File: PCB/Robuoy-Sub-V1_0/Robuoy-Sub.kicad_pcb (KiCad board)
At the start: 4 copper layers, 100 x 80 mm, 160 parts, among them J101 1051330011, J102 Display, J103 LEDSTRIP, J104 SW1, J105 SW2, J201 Accu, J202 ESC SB POWER, J203 ESC BB POWER, J401 ESC-BB, J402 ESC-SB, J501 GPS, J601 Conn_Coaxial, J701 LED1, J702 LED2, J703 LED3, J704 SW1, J705 SW3, J706 SW2, J707 3.3V switch, J708 Vbatt switch, J709 MainswitchLeds, J901 Display, Q101 2N7002, Q102 2N7002, Q201 NCE01P30K, Q701 MMBT5551L, Q702 MMBT5551L, Q703 MMBT5551L, Q704 MMBT5551L, SW101 ~{BOOT}, SW102 ~{RESET}, SW201 ON/OFF, U101 SRV05-4, U102 CP2104-F03-GMR, U103 ESP32-WROOM-32E_(visible_peri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, U201 AP7363, U202 XL1509-5.0E1, U301 LSM303C, U601 Ai-Thinker-Ra-01, U701 MCP23017_SS, U801 LIS2HH12

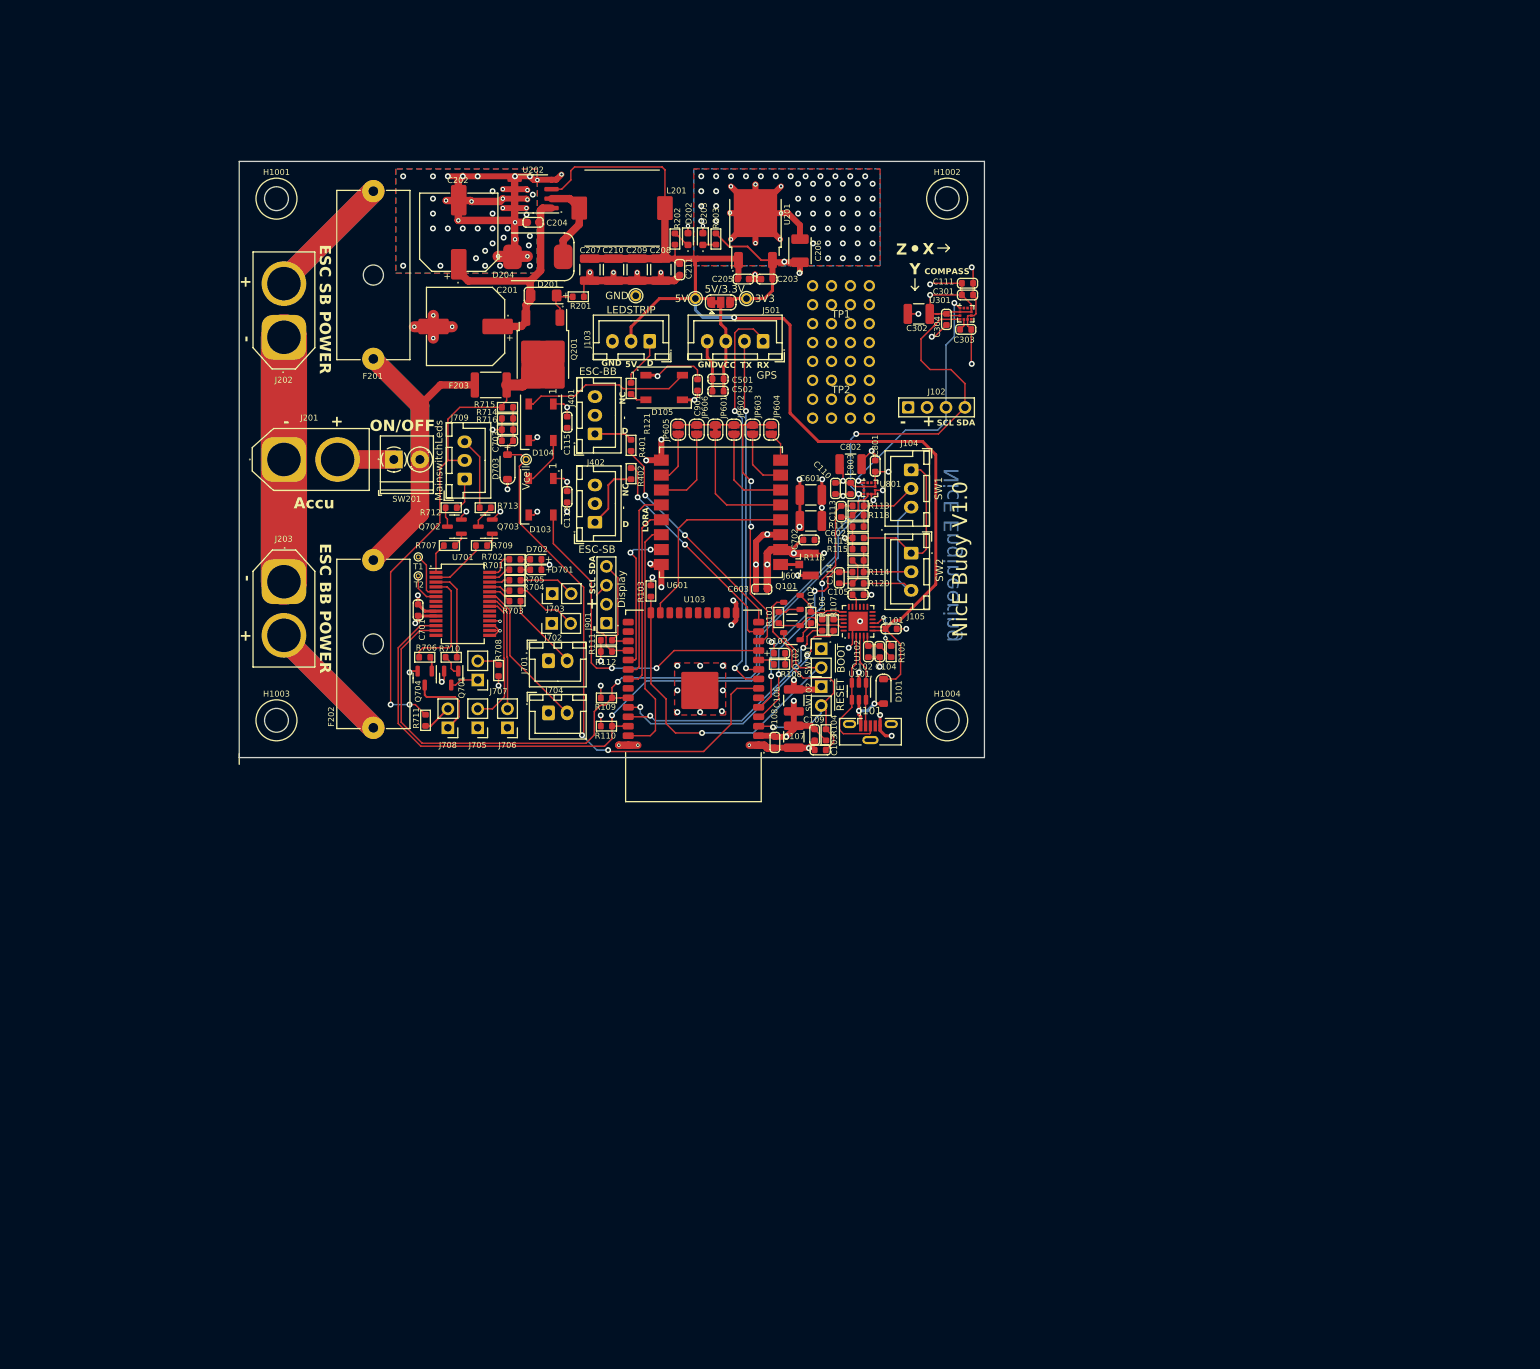
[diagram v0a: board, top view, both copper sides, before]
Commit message: Sub ready for routing
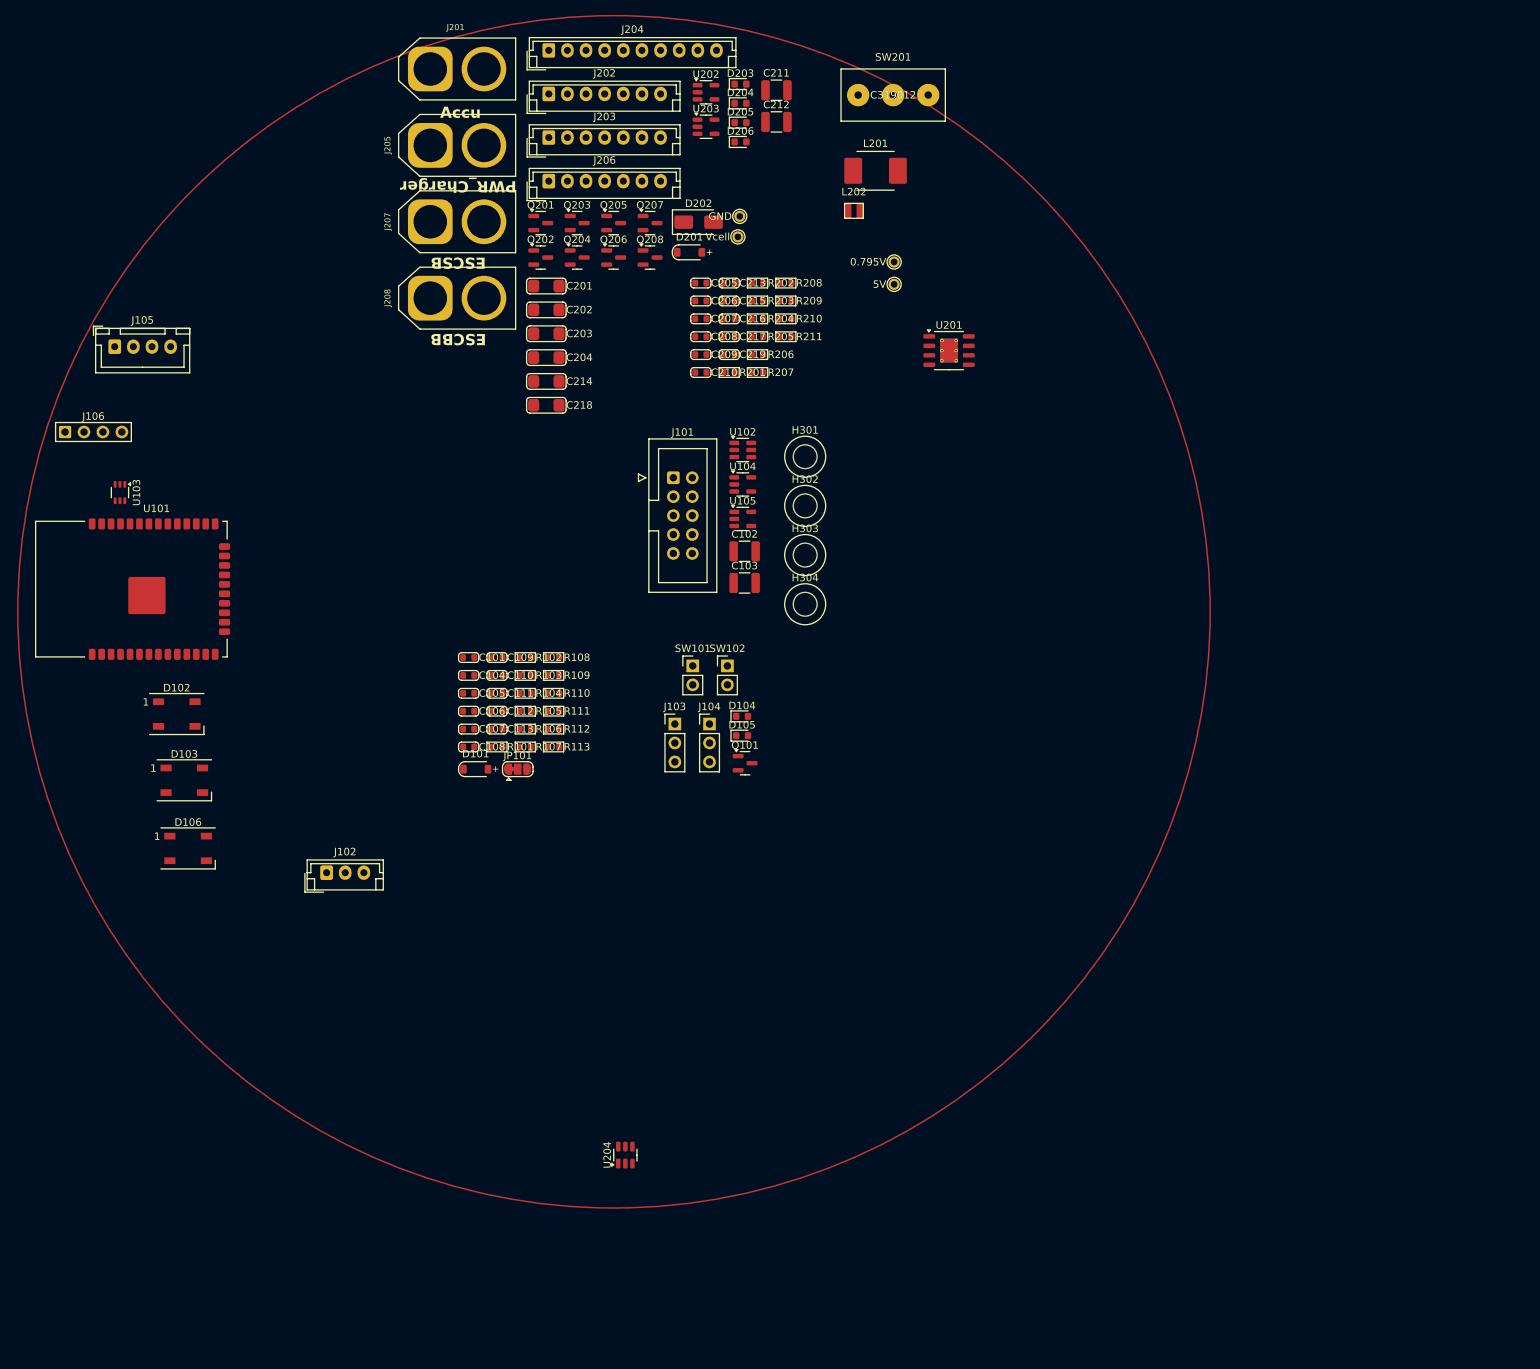
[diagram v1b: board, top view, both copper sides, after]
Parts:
- removed C114, C703: 1n, A_Device:C_0603
- removed C115, C301, C303, C304, C501, C502, C603, C701, C702, C801, C803, C901: 100n, A_Device:C_0603
- removed C302, C802: 10u, Capacitor_SMD:C_1210_3225Metric
- removed C601, C602: 100u/16V, Capacitor_SMD:C_1210_3225Metric
- removed D701: GREEN, A_Device:LED_0603
- removed D702: RED, A_Device:LED_0603
- removed D703: SM4007PL, A_Device:D_SOD-123_2.85x1.8x1.3
- removed F201, F202: 10A/T, Fuse:Fuseholder_Cylinder-5x20mm_Schurter_0031_8201_Horizontal_Open
- removed F203: 3AT, Fuse:Fuse_1812_4532Metric
- removed H1001, H1002, H1003, H1004: MountingHole, A_Mechanical:NPTH_M3
- removed J401: ESC-BB, Connector_JST:JST_XH_B3B-XH-A_1x03_P2.50mm_Vertical
- removed J402: ESC-SB, Connector_JST:JST_XH_B3B-XH-A_1x03_P2.50mm_Vertical
- removed J501: GPS, Connector_JST:JST_XH_B4B-XH-A_1x04_P2.50mm_Vertical
- removed J601: Conn_Coaxial, Connector_Coaxial:U.FL_Hirose_U.FL-R-SMT-1_Vertical
- removed J701: LED1, Connector_JST:JST_XH_B2B-XH-A_1x02_P2.50mm_Vertical
- removed J702: LED2, Connector_PinHeader_2.54mm:PinHeader_1x02_P2.54mm_Vertical
- removed J703: LED3, Connector_PinHeader_2.54mm:PinHeader_1x02_P2.54mm_Vertical
- removed J704: SW1, Connector_JST:JST_XH_B2B-XH-A_1x02_P2.50mm_Vertical
- removed J705: SW3, Connector_PinHeader_2.54mm:PinHeader_1x02_P2.54mm_Vertical
- removed J706: SW2, Connector_PinHeader_2.54mm:PinHeader_1x02_P2.54mm_Vertical
- removed J707: 3.3V switch, Connector_PinHeader_2.54mm:PinHeader_1x02_P2.54mm_Vertical
- removed J708: Vbatt switch, Connector_PinHeader_2.54mm:PinHeader_1x02_P2.54mm_Vertical
- removed J709: MainswitchLeds, Connector_JST:JST_XH_B3B-XH-A_1x03_P2.50mm_Vertical
- removed J901: Display, A_Connector:Header_1x04_P2.54_Male
- removed JP501: 5V/3.3V, Jumper:SolderJumper-3_P1.3mm_Bridged12_RoundedPad1.0x1.5mm
- removed JP601: D0, Jumper:SolderJumper-2_P1.3mm_Bridged_RoundedPad1.0x1.5mm
- removed JP602: D1, Jumper:SolderJumper-2_P1.3mm_Open_RoundedPad1.0x1.5mm
- removed JP603: D2, Jumper:SolderJumper-2_P1.3mm_Open_RoundedPad1.0x1.5mm
- removed JP604: D3, Jumper:SolderJumper-2_P1.3mm_Open_RoundedPad1.0x1.5mm
- removed JP605: D4, Jumper:SolderJumper-2_P1.3mm_Open_RoundedPad1.0x1.5mm
- removed JP606: D5, Jumper:SolderJumper-2_P1.3mm_Open_RoundedPad1.0x1.5mm
- removed Q102: 2N7002, A_IC_SOT:SOT-23_1.4x3_P0.95
- removed Q701, Q702, Q703, Q704: MMBT5551L, Package_TO_SOT_SMD:SOT-23
- removed R114, R119, R120, R121, R401, R402, R703, R704, R705, R708, R711: 100, A_Device:R_0603
- removed R115, R116, R117, R118: 10K, A_Device:R_0603
- removed R701, R702, R706, R707, R709, R710, R714, R716: 1k, A_Device:R_0603
- removed R712, R713: 4.7k, A_Device:R_0603
- removed R715: 6.2k, A_Device:R_0603
- removed TP1: RW1, A_Misc:ReworkPins
- removed TP2: RW2, A_Misc:ReworkPins
- removed TP701: Vcell, A_Pads_Pins:Testpoint_0.6x1.0
- removed TP702: T1, A_Pads_Pins:Testpoint_0.4x0.7
- removed TP703: T2, A_Pads_Pins:Testpoint_0.4x0.7
- removed U301: LSM303C, Package_LGA:LGA-12_2x2mm_P0.5mm
- removed U601: Ai-Thinker-Ra-01, RF_Module:Ai-Thinker-Ra-01-LoRa
- removed U701: MCP23017_SS, Package_SO:SSOP-28_5.3x10.2mm_P0.65mm
- removed U801: LIS2HH12, Package_LGA:LGA-12_2x2mm_P0.5mm
- added C212: 100u/16V, Capacitor_SMD:C_1210_3225Metric, F.Cu at (116.6, 30.1)
- added C213: 100n, A_Device:C_0603, F.Cu at (110.3, 51.7)
- added C214: 4.7uF/10V, A_Device:C_1206_(1.6), F.Cu at (85.7, 64.9)
- added C215: 100n, A_Device:C_0603, F.Cu at (110.3, 54.1)
- added C216: 100n, A_Device:C_0603, F.Cu at (110.3, 56.5)
- added C217: 100n, A_Device:C_0603, F.Cu at (110.3, 58.9)
- added C218: 4.7uF/10V, A_Device:C_1206_(1.6), F.Cu at (85.7, 68.1)
- added C219: 100n, A_Device:C_0603, F.Cu at (110.3, 61.3)
- added D106: WS2812B, LED_SMD:LED_WS2812B_PLCC4_5.0x5.0mm_P3.2mm, F.Cu at (37.7, 127.6)
- added D205: ESC_BB, LED_SMD:LED_0603_1608Metric, F.Cu at (111.8, 30.2)
- added D206: ESC_SB, LED_SMD:LED_0603_1608Metric, F.Cu at (111.8, 32.8)
- added H301: MountingHole, A_Mechanical:NPTH_M3, F.Cu at (120.5, 75.0)
- added H302: MountingHole, A_Mechanical:NPTH_M3, F.Cu at (120.5, 81.6)
- added H303: MountingHole, A_Mechanical:NPTH_M3, F.Cu at (120.5, 88.2)
- added H304: MountingHole, A_Mechanical:NPTH_M3, F.Cu at (120.5, 94.8)
- added J106: Compass, A_Connector:Header_1x04_P2.54_Male, F.Cu at (25.0, 71.7)
- added J204: Conn_01x10, Connector_JST:JST_EH_B10B-EH-A_1x10_P2.50mm_Vertical, F.Cu at (86.1, 20.5)
- added J205: PWR_Charger, A_Connector:AMASS_XT60-F_1x02_P7.20mm_Vertical, F.Cu at (70.2, 33.2)
- added J206: LoadbalanceCharger, Connector_JST:JST_EH_B7B-EH-A_1x07_P2.50mm_Vertical, F.Cu at (86.1, 38.0)
- added J207: ESCSB, A_Connector:AMASS_XT60-F_1x02_P7.20mm_Vertical, F.Cu at (70.2, 43.5)
- added J208: ESCBB, A_Connector:AMASS_XT60-F_1x02_P7.20mm_Vertical, F.Cu at (70.2, 53.7)
- added JP101: 5V/3.3V, Jumper:SolderJumper-3_P1.3mm_Bridged12_RoundedPad1.0x1.5mm, F.Cu at (81.9, 116.9)
- added L202: 10uH, A_Device:FTC252012S, F.Cu at (127.0, 42.0)
- added Q202: AO3400A, Package_TO_SOT_SMD:SOT-23, F.Cu at (85.0, 48.3)
- added Q203: AO3400A, Package_TO_SOT_SMD:SOT-23, F.Cu at (89.9, 43.7)
- added Q204: AO3400A, Package_TO_SOT_SMD:SOT-23, F.Cu at (89.9, 48.3)
- added Q205: AO3400A, Package_TO_SOT_SMD:SOT-23, F.Cu at (94.8, 43.7)
- added Q206: AO3400A, Package_TO_SOT_SMD:SOT-23, F.Cu at (94.8, 48.3)
- added Q207: AO3400A, Package_TO_SOT_SMD:SOT-23, F.Cu at (99.6, 43.7)
- added Q208: AO3400A, Package_TO_SOT_SMD:SOT-23, F.Cu at (99.6, 48.3)
- added R204: 18K, A_Device:R_0603, F.Cu at (114.1, 56.5)
- added R205: 10K, A_Device:R_0603, F.Cu at (114.1, 58.9)
- added R206: 1.8k, A_Device:R_0603, F.Cu at (114.1, 61.3)
- added R207: 1k, A_Device:R_0603, F.Cu at (114.1, 63.7)
- added R208: 1.8k, A_Device:R_0603, F.Cu at (117.9, 51.7)
- added R209: 1.8k, A_Device:R_0603, F.Cu at (117.9, 54.1)
- added R210: 82K, A_Device:R_0603, F.Cu at (117.9, 56.5)
- added R211: 15K, A_Device:R_0603, F.Cu at (117.9, 58.9)
- added TP204: 5V, A_Pads_Pins:Testpoint_0.9x1.5, F.Cu at (132.4, 51.9)
- added U104: SN74LV1T34DBV, Package_TO_SOT_SMD:SOT-23-5, F.Cu at (112.1, 78.7)
- added U105: SN74LV1T34DBV, Package_TO_SOT_SMD:SOT-23-5, F.Cu at (112.1, 83.4)
- added U203: SN74LV1T34DBV, Package_TO_SOT_SMD:SOT-23-5, F.Cu at (107.2, 30.7)
- added U204: TLV61046ADB, Package_TO_SOT_SMD:SOT-23-6, F.Cu at (96.3, 168.7)
- C101, C105: value 4.7u -> 100n
- C102: value 4.7u -> 100u/16V; footprint A_Device:C_0603 -> Capacitor_SMD:C_1210_3225Metric
- C103, C211: value 100n -> 100u/16V; footprint A_Device:C_0603 -> Capacitor_SMD:C_1210_3225Metric
- C106, C107, C207, C209, C210: value 100u/16V -> 100n; footprint Capacitor_SMD:C_1210_3225Metric -> A_Device:C_0603
- C112: value 100n -> 10n
- C113: value 1n -> 100n
- C201, C202: value 220u/50V -> 4.7uF/10V; footprint A_Device:CP_ALU_D10x10.5 -> A_Device:C_1206_(1.6)
- C203, C204: value 100n -> 4.7uF/10V; footprint A_Device:C_0603 -> A_Device:C_1206_(1.6)
- C206: value 100u/6.3V -> 10n; footprint A_Device:CP_TANT_3.5x2.8x1.9 -> A_Device:C_0603
- C208: value 100u/16V -> 10n; footprint Capacitor_SMD:C_1210_3225Metric -> A_Device:C_0603
- D102: value GREEN -> WS2812B; footprint A_Device:LED_0603 -> LED_SMD:LED_WS2812B_PLCC4_5.0x5.0mm_P3.2mm
- D104, D105: value WS2812B -> PWR_ESC_BB; footprint LED_SMD:LED_WS2812B_PLCC4_5.0x5.0mm_P3.2mm -> LED_SMD:LED_0603_1608Metric
- D201: value ZMM5V6-M -> SM4007PL; footprint A_Device:D_MiniMELF -> A_Device:D_SOD-123_2.85x1.8x1.3
- D202: value 5V -> B340A; footprint LED_SMD:LED_0603_1608Metric -> Diode_SMD:D_SMA
- D203: value 3.3V -> 5V
- D204: value SS36-E3/57T -> 3.3V; footprint A_Device:D_SMC_7.1x6.2x2.65 -> LED_SMD:LED_0603_1608Metric
- J101: value 1051330011 -> PROG/JTAG; footprint Connector_USB:USB_Micro-B_Molex-105133-0001 -> Connector_IDC:IDC-Header_2x05_P2.54mm_Vertical
- J102: value Display -> TO PUSH BUTTON; footprint A_Connector:Header_1x04_P2.54_Male -> Connector_JST:JST_EH_B3B-EH-A_1x03_P2.50mm_Vertical
- J103: value LEDSTRIP -> ESC_BB; footprint Connector_JST:JST_XH_B3B-XH-A_1x03_P2.50mm_Vertical -> Connector_PinHeader_2.54mm:PinHeader_1x03_P2.54mm_Vertical
- J104: value SW1 -> ESC_SB; footprint Connector_JST:JST_XH_B3B-XH-A_1x03_P2.50mm_Vertical -> Connector_PinHeader_2.54mm:PinHeader_1x03_P2.54mm_Vertical
- J105: value SW2 -> RS232_Option; footprint Connector_JST:JST_XH_B3B-XH-A_1x03_P2.50mm_Vertical -> Connector_JST:JST_XH_B4B-XH-A_1x04_P2.50mm_Vertical
- J202: value ESC SB POWER -> LoadbalanceAccu1; footprint A_Connector:AMASS_XT60-F_1x02_P7.20mm_Vertical -> Connector_JST:JST_EH_B7B-EH-A_1x07_P2.50mm_Vertical
- J203: value ESC BB POWER -> LoadbalanceAccu2; footprint A_Connector:AMASS_XT60-F_1x02_P7.20mm_Vertical -> Connector_JST:JST_EH_B7B-EH-A_1x07_P2.50mm_Vertical
- L201: value 68uH/3A -> 33uH/2A; footprint A_Device:L_11.5x10.0mm -> A_Device:L_6.6x7.0mm
- Q101: value 2N7002 -> AO3400A; footprint A_IC_SOT:SOT-23_1.4x3_P0.95 -> Package_TO_SOT_SMD:SOT-23
- Q201: value NCE01P30K -> AO3400A; footprint Package_TO_SOT_SMD:TO-252-2 -> Package_TO_SOT_SMD:SOT-23
- R103, R104, R105: value 10K -> 100
- R106: value 120E -> 100
- R107: value 120E -> 820
- R108: value 1k -> 2.2k
- R110, R111: value 2.2k -> 100
- R112: value 2.2k -> 1.8k
- R113: value 100 -> 1.8k
- R201: value 100 -> 1k
- R202: value 1.5k -> 6.2k
- SW201: value ON/OFF -> SS-12D11-G050/On-Off; footprint TerminalBlock_Phoenix:TerminalBlock_Phoenix_PT-1,5-2-3.5-H_1x02_P3.50mm_Horizontal -> A_Connector:SS-12D10L5
- TP201: value GND -> Vcell
- TP202: value 3V3 -> GND
- TP203: value 5V -> 0.795V
- U101: value SRV05-4 -> ESP32-WROOM-32E_(visible_peripherals); footprint Package_TO_SOT_SMD:SOT-23-6 -> A_Module:ESP32-WROOM-32
- U102: value CP2104-F03-GMR -> USBLC6-4SC6; footprint Package_DFN_QFN:QFN-24-1EP_4x4mm_P0.5mm_EP2.6x2.6mm -> Package_TO_SOT_SMD:SOT-23-6
- U103: value ESP32-WROOM-32E_(visible_peripherals) -> LTC4311; footprint A_Module:ESP32-WROOM-32 -> Package_TO_SOT_SMD:Texas_R-PDSO-G6
- U201: value AP7363 -> TPS5430DDAR; footprint Package_TO_SOT_SMD:TO-252-2 -> Package_SO:HTSOP-8-1EP_3.9x4.9mm_P1.27mm_EP2.4x3.2mm_ThermalVias
- U202: value XL1509-5.0E1 -> SN74LV1T34DBV; footprint Package_SO:SOIC-8_3.9x4.9mm_P1.27mm -> Package_TO_SOT_SMD:SOT-23-5
- moved J105 110.4 mm to (27.8, 60.3), turned to 0 degrees
- moved J102 102.9 mm to (56.2, 130.8)
- moved U101 98.6 mm to (30.0, 92.8), turned to 0 degrees
- moved U103 84.7 mm to (28.5, 79.8), turned to -90 degrees
- moved C111 83.8 mm to (79.1, 106.8)
- moved SW201 83.0 mm to (132.3, 26.5)
- moved D102 81.3 mm to (36.1, 109.5), turned to 0 degrees
- moved J203 69.4 mm to (86.1, 32.2), turned to 0 degrees
- moved D103 61.1 mm to (37.1, 118.4), turned to 0 degrees
- moved C101 56.8 mm to (75.3, 102.0), turned to 0 degrees
- moved J201 56.0 mm to (70.2, 23.0)
- moved D101 55.7 mm to (76.2, 116.9), turned to 0 degrees
- moved C104 55.3 mm to (75.3, 104.4), turned to 0 degrees
- moved C113 54.6 mm to (79.1, 111.6), turned to 0 degrees
- moved C105 53.9 mm to (75.3, 106.8), turned to 0 degrees
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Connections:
- C101 pad 1: GND -> EN
- C101 pad 2: +5V -> GND
- C102 pad 1: GND -> +3.3V
- C102 pad 2: Net-(U102-VDD) -> GND
- C103 pad 1: EN -> +3.3V
- C104 pad 1: GND -> +3.3V
- C104 pad 2: Net-(U102-VDD) -> GND
- C105 pad 1: GND -> +3.3V
- C105 pad 2: Net-(U102-VPP) -> GND
- C110 pad 1: +3.3V -> +5V
- C111 pad 1: +3.3V -> +5V
- C112 pad 1: +3.3V -> GND
- C112 pad 2: GND -> BUTTON
- C113 pad 1: Net-(U103-GPIO36) -> +3.3V
- C201 pad 1: Net-(D201-K) -> +VSW
- C202 pad 1: Net-(D201-K) -> +VSW
- C203 pad 1: +5V -> +VSW
- C204 pad 1: Net-(D201-K) -> +VSW
- C205 pad 1: +3.3V -> +VSW
- C206 pad 1: +3.3V -> +VSW
- C207 pad 1: +5V -> Vbatt
- C208 pad 1: +5V -> Net-(D202-K)
- C208 pad 2: GND -> Net-(U201-BOOT)
- C211 pad 1: +5V -> +3.3V
- D101 pad 1: +5V -> +3.3V
- D101 pad 2: Net-(D101-A) -> BUTTON
- D102 pad 1: Net-(D102-K) -> +3.3V
- D102 pad 2: +3.3V -> Net-(D102-DOUT)
- D103 pad 4: /CPU/LEDS -> Net-(D102-DOUT)
- D104 pad 1: +3.3V -> GND
- D104 pad 2: Net-(D104-DOUT) -> Net-(D104-A)
- D105 pad 1: +3.3V -> GND
- D105 pad 2: Net-(D105-DOUT) -> Net-(D105-A)
- D201 pad 1: Net-(D201-K) -> +3.3V
- D201 pad 2: Net-(D201-A) -> Vbatt
- D202 pad 1: GND -> Net-(D202-K)
- D202 pad 2: Net-(D202-A) -> GND
- D204 pad 1: Net-(D204-K) -> GND
- D204 pad 2: GND -> Net-(D204-A)
- J101 pad 1: Net-(D101-A) -> EN
- J101 pad 2: Net-(J101-D-) -> +3.3V
- J101 pad 3: Net-(J101-D+) -> TX
- J101 pad 4: unconnected-(J101-ID-Pad4) -> GND
- J101 pad 5: GND -> RX
- J101 pad 6: unconnected-(J101-Shield-Pad6) -> DR0
- J102 pad 1: GND -> Net-(J102-Pin_1)
- J102 pad 3: /CPU/SCL -> Net-(J102-Pin_3)
- J103 pad 2: +5V -> Net-(J103-Pin_2)
- J104 pad 3: Net-(J104-Pin_3) -> GND
- J105 pad 1: Net-(J104-Pin_1) -> Net-(J105-Pin_1)
- J105 pad 3: Net-(J104-Pin_3) -> /CPU/Vext
- J201 pad 2: /PSU/ACC -> Vbatt
- J202 pad 1: GND -> Net-(J202-Pin_1)
- J203 pad 1: GND -> Net-(J202-Pin_1)
- J203 pad 2: Net-(J203-Pin_2) -> Net-(J202-Pin_2)
- L201 pad 1: Net-(D204-K) -> Net-(D202-K)
- L201 pad 2: +5V -> +3.3V
- Q101 pad 1: Net-(Q101-B) -> BUTTON_LIGHT
- Q101 pad 2: RTS -> GND
- Q101 pad 3: EN -> Net-(Q101-D)
- Q201 pad 1: Net-(D201-A) -> Net-(Q201-G)
- Q201 pad 2: +28V -> GND
- Q201 pad 3: Net-(D201-K) -> Net-(D205-K)
- R101 pad 1: Net-(Q101-B) -> +3.3V
- R101 pad 2: DTR -> DR0
- R102 pad 1: Net-(Q102-B) -> +3.3V
- R102 pad 2: RTS -> EN
- R103 pad 1: +3.3V -> Net-(J101-Pin_7)
- R103 pad 2: DR0 -> MTMS
- R104 pad 1: +3.3V -> Net-(J101-Pin_8)
- R104 pad 2: EN -> MTCK
- R105 pad 1: Net-(U102-VDD) -> Net-(J101-Pin_9)
- R105 pad 2: Net-(U102-~{RSTb}) -> MTDO
- R106 pad 1: TX -> Net-(J101-Pin_10)
- R106 pad 2: Net-(U102-RXD) -> MTDI
- R107 pad 1: RX -> BUTTON
- R107 pad 2: Net-(U102-TXD) -> GND
- R108 pad 1: Net-(U103-GPIO25) -> +3.3V
- R108 pad 2: Net-(D102-K) -> /CPU/SDA
- R109 pad 2: /CPU/SDA -> /CPU/SCL
- R110 pad 1: +3.3V -> BUTTON
- R110 pad 2: /CPU/SCL -> Net-(J102-Pin_3)
- R111 pad 1: +3.3V -> Net-(Q101-D)
- R111 pad 2: /CPU/SDA_DISP -> Net-(J102-Pin_1)
- R112 pad 1: +3.3V -> Net-(D104-A)
- R112 pad 2: /CPU/SCL_DISP -> Net-(J103-Pin_2)
- R113 pad 1: Net-(U103-GPIO36) -> Net-(D105-A)
- R201 pad 1: GND -> Vbatt
- R201 pad 2: Net-(D201-A) -> GND
- R202 pad 1: +5V -> +VSW
- R202 pad 2: Net-(D202-A) -> Vbatt
- R203 pad 1: Net-(D203-A) -> Vbatt
- R203 pad 2: +3.3V -> GND
- SW201 pad 1: /PSU/ACC -> Vbatt
- SW201 pad 2: /PSU/POWER -> +VSW
- TP201 pad 1: GND -> Vbatt
- TP202 pad 1: +3.3V -> GND
- TP203 pad 1: +5V -> Net-(U204-FB)
- U101 pad 1: Net-(J101-D-) -> GND
- U101 pad 2: GND -> +3.3V
- U101 pad 3: Net-(J101-D+) -> EN
- U101 pad 4: Net-(J101-D+) -> unconnected-(U101-GPIO36-Pad4)
- U101 pad 5: Net-(D101-A) -> unconnected-(U101-GPIO39-Pad5)
- U101 pad 6: Net-(J101-D-) -> unconnected-(U101-GPIO34-Pad6)
- U102 pad 1: unconnected-(U102-RI/CLK-Pad1) -> Net-(J105-Pin_2)
- U102 pad 3: Net-(J101-D+) -> Net-(J105-Pin_1)
- U102 pad 4: Net-(J101-D-) -> /CPU/SDA
- U102 pad 5: Net-(U102-VDD) -> +3.3V
- U102 pad 6: Net-(U102-VDD) -> /CPU/SCL
- U103 pad 1: GND -> +3.3V
- U103 pad 2: +3.3V -> GND
- U103 pad 3: EN -> +3.3V
- U103 pad 4: Net-(U103-GPIO36) -> /CPU/SCL
- U103 pad 5: Net-(U103-GPIO39) -> GND
- U103 pad 6: unconnected-(U103-GPIO34-Pad6) -> /CPU/SDA
- U201 pad 1: +5V -> Net-(U201-BOOT)
- U201 pad 2: GND -> unconnected-(U201-NC-Pad2)
- U201 pad 3: +3.3V -> unconnected-(U201-NC-Pad3)
- U202 pad 1: Net-(D201-K) -> unconnected-(U202-NC-Pad1)
- U202 pad 2: Net-(D204-K) -> /CPU/PWR_ESC_SB
- U202 pad 3: +5V -> GND
- U202 pad 4: GND -> Net-(Q201-G)
- U202 pad 5: GND -> +5V
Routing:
- net GND: track 338.8 -> 0.00 mm, vias 166 -> 0
- net +5V: track 170.0 -> 0.00 mm, vias 1 -> 0
- net /CPU/SDA: track 147.9 -> 0.00 mm, vias 3 -> 0
- net /CPU/SCL: track 139.9 -> 0.00 mm, vias 3 -> 0
- net +3.3V: track 129.8 -> 0.00 mm, vias 26 -> 0
- net /Accumonitor/Vbatt: track 80.9 -> 0.00 mm, vias 2 -> 0
- net +28V: track 66.1 -> 0.00 mm, vias 2 -> 0
- net /PSU/POWER: track 56.8 -> 0.00 mm
- net /CPU/GPSRX: track 54.5 -> 0.00 mm, vias 2 -> 0
- net DR0: track 51.3 -> 0.00 mm, vias 1 -> 0
- net /CPU/GPSTX: track 45.7 -> 0.00 mm, vias 2 -> 0
- net /CPU/LEDS: track 45.7 -> 0.00 mm, vias 2 -> 0
- net /CPU/RADIO_6: track 45.2 -> 0.00 mm, vias 2 -> 0
- net EN: track 38.5 -> 0.00 mm, vias 1 -> 0
- net RX: track 35.5 -> 0.00 mm, vias 2 -> 0
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- removed copper zone on In2.Cu, net +3.3V
- removed copper zone on B.Cu, net GND
- removed copper zone on F.Cu, net GND
- removed copper zone on In1.Cu, net GND
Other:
- board outline removed
- board text removed: "+"
- board text removed: "-"
- board text removed: "5V"
- board text removed: "COMPASS"
- board text removed: "D"
- board text removed: "GND"
- board text removed: "LORA"
- board text removed: "NC"
- board text removed: "NicE Buoy V1.0"
- board text removed: "NicE Engineering"
- board text removed: "RX"
- board text removed: "SCL"
- board text removed: "SDA"
- board text removed: "TX"
- board text removed: "VCC"
- board text removed: "X"
- board text removed: "Y"
- board text removed: "Z"

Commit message: Pcb's getting ready for routing
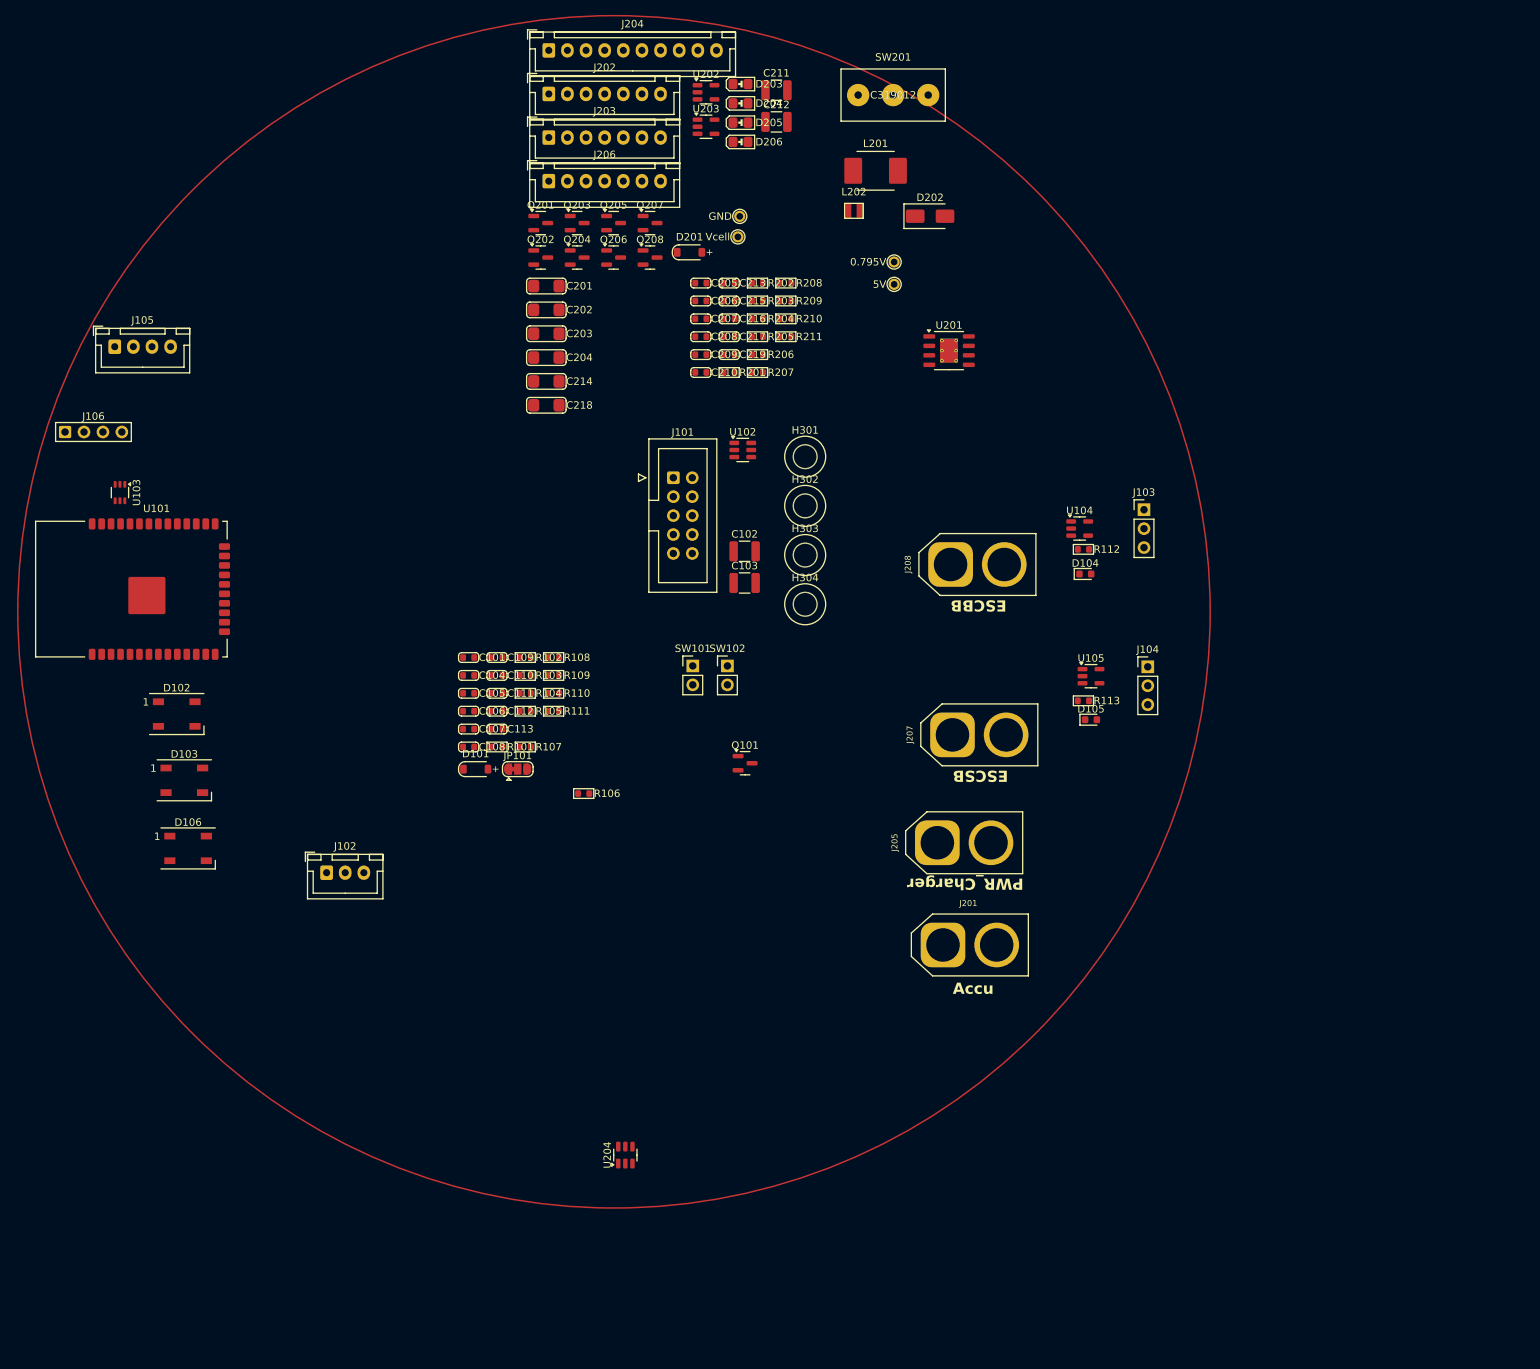
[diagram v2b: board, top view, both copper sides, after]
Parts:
- D203, D204, D205, D206: footprint LED_SMD:LED_0603_1608Metric -> A_Passive:LED_0805
- J102: footprint Connector_JST:JST_EH_B3B-EH-A_1x03_P2.50mm_Vertical -> Connector_JST:JST_XH_B3B-XH-A_1x03_P2.50mm_Vertical
- J202, J203, J206: footprint Connector_JST:JST_EH_B7B-EH-A_1x07_P2.50mm_Vertical -> Connector_JST:JST_XH_B7B-XH-A_1x07_P2.50mm_Vertical
- J204: footprint Connector_JST:JST_EH_B10B-EH-A_1x10_P2.50mm_Vertical -> Connector_JST:JST_XH_B10B-XH-A_1x10_P2.50mm_Vertical
- moved J201 136.2 mm to (139.0, 140.5)
- moved J205 115.7 mm to (138.2, 126.8)
- moved J207 98.2 mm to (140.2, 112.3)
- moved J208 78.4 mm to (140.0, 89.5)
- moved R112 75.1 mm to (157.8, 87.5)
- moved R113 71.4 mm to (157.8, 107.8)
- moved J103 69.2 mm to (165.9, 82.1)
- moved J104 59.3 mm to (166.4, 103.2)
- moved U105 51.3 mm to (158.8, 104.5)
- moved D104 49.9 mm to (158.0, 90.8)
- moved D105 46.9 mm to (158.8, 110.3)
- moved U104 45.6 mm to (157.3, 84.7)
- moved D202 31.1 mm to (137.2, 42.7)
- moved R106 11.7 mm to (90.7, 120.2)
